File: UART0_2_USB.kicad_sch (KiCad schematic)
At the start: 5 parts, among them J6 USB_C_16P, U6 CH340E

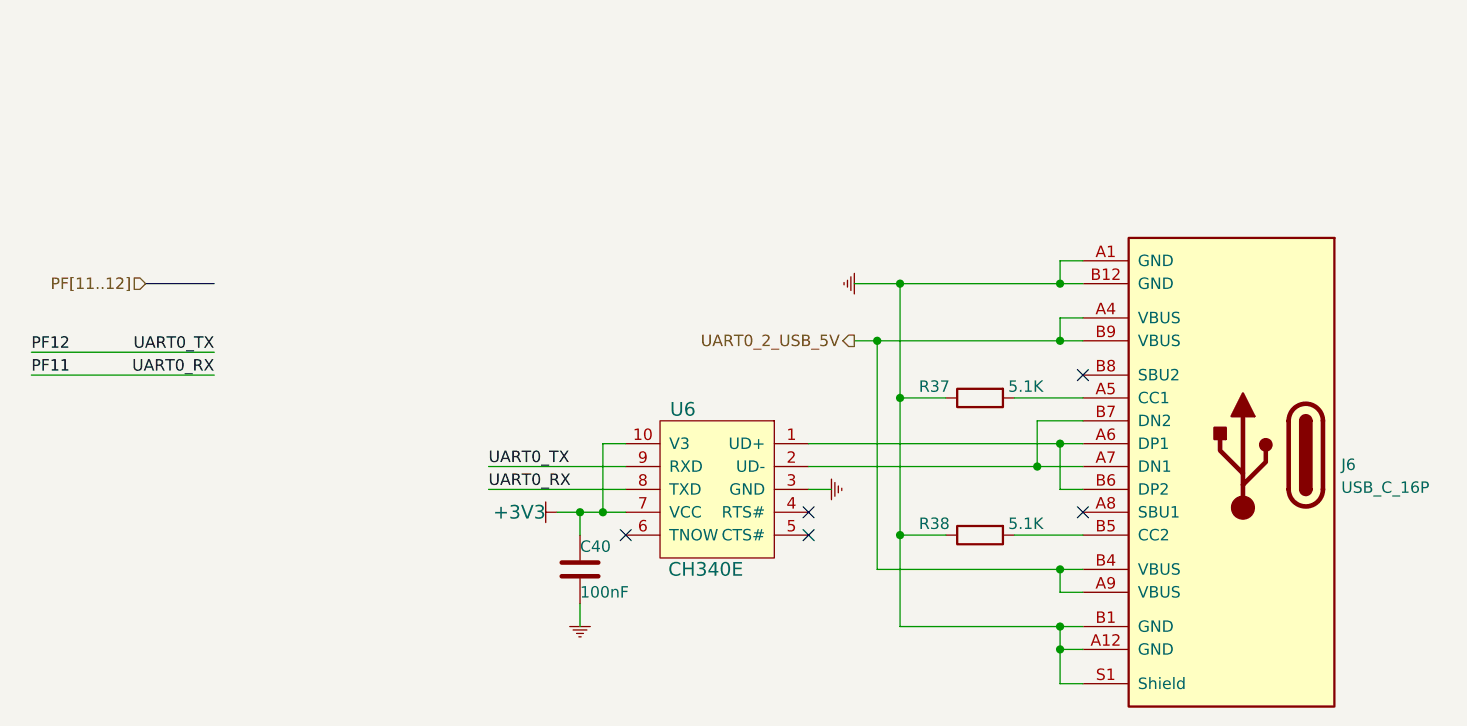
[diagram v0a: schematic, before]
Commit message: update schematic and footprints
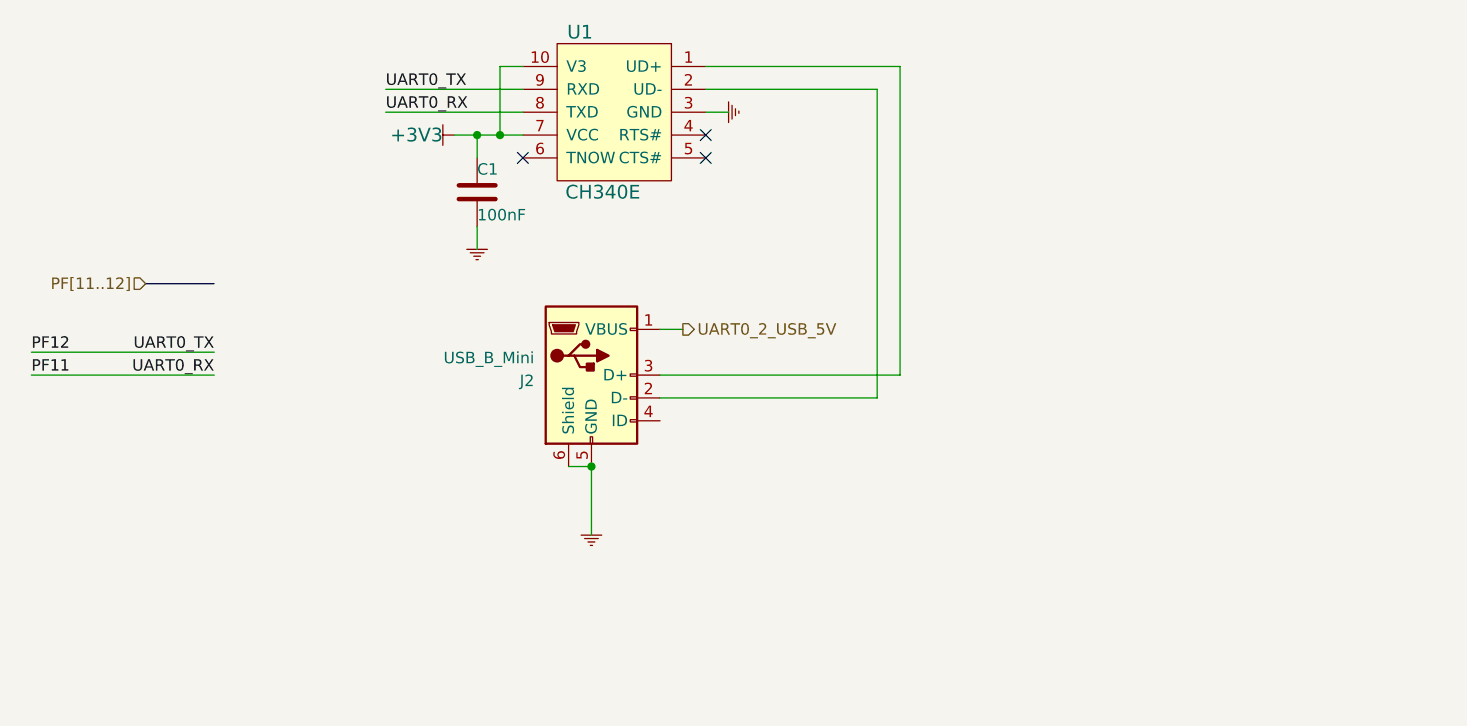
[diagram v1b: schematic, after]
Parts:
- removed C40: 100nF, Capacitor_SMD:C_0603_1608Metric, symbol Device:C
- removed J6: USB_C_16P, 0_ungrouped:USB_C_16P_4Foot8.64mm, symbol 0_ungrouped:USB_C_16P
- removed R37, R38: 5.1K, Resistor_SMD:R_0603_1608Metric, symbol Device:R
- removed U6: CH340E, Package_SO:MSOP-10_3x3mm_P0.5mm, symbol 0_ungrouped:CH340E
- added C1: 100nF, Capacitor_SMD:C_0805_2012Metric_Pad1.18x1.45mm_HandSolder, symbol Device:C
- added J2: USB_B_Mini, digikey-footprints:USB_Mini_B_Female_690-005-299-043, symbol Connector:USB_B_Mini
- added U1: CH340E, Package_SO:MSOP-10_3x3mm_P0.5mm, symbol 0_ungrouped:CH340E
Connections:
- net +3V3: now also C1.1, U1.10 (V3), U1.7 (VCC)
- net GND: now also C1.2, J2.5 (GND), J2.6 (Shield), U1.3 (GND)
- net PF11: now also U1.8 (TXD)
- net PF12: now also U1.9 (RXD)
- net UART0_2_USB_5V: now also J2.1 (VBUS)
- new net: J2.2 (D-), U1.2 (UD-)
- new net: J2.3 (D+), U1.1 (UD+)
- no-connect marks 5 -> 3
